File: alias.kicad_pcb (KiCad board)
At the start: 2 copper layers, 84.2 x 38.1 mm, 24 parts, among them SW1 SW_Push, U1 ATmega32U4-A, Y1 16MHz

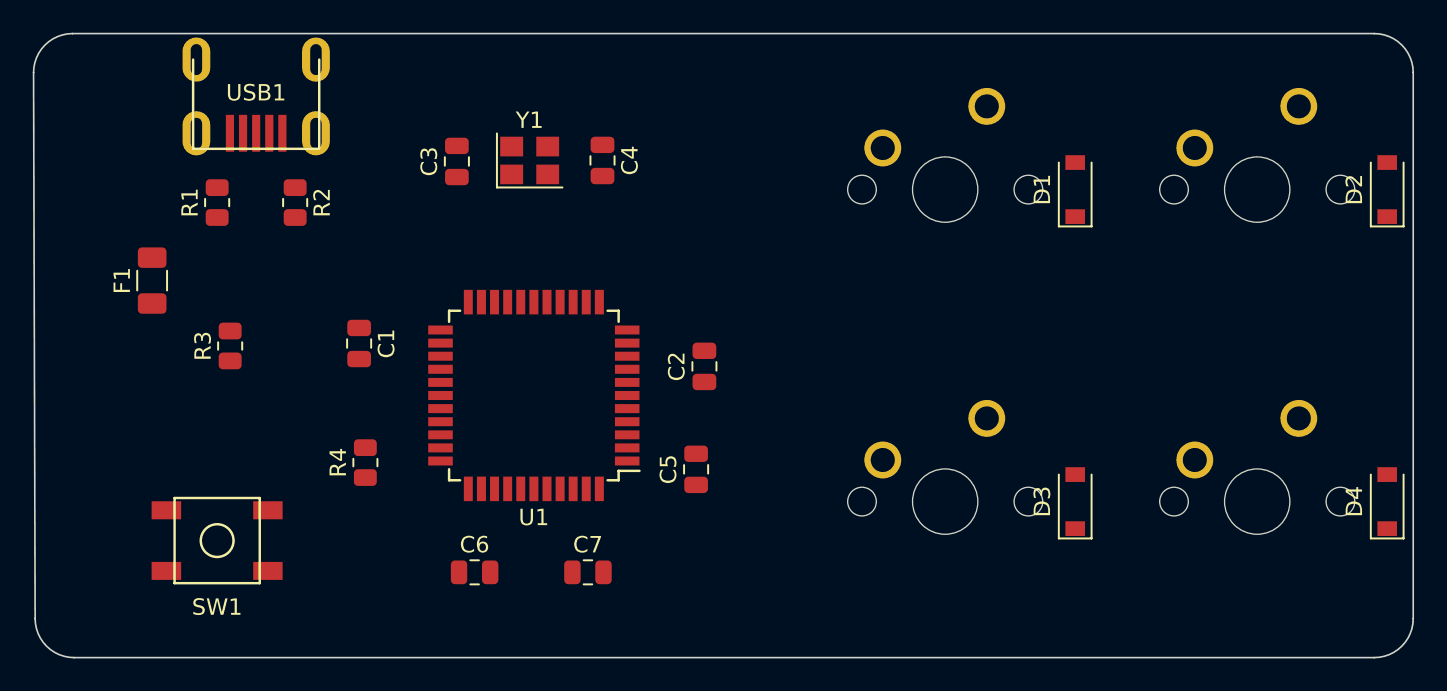
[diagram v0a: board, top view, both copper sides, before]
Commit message: Added routing (not finished)
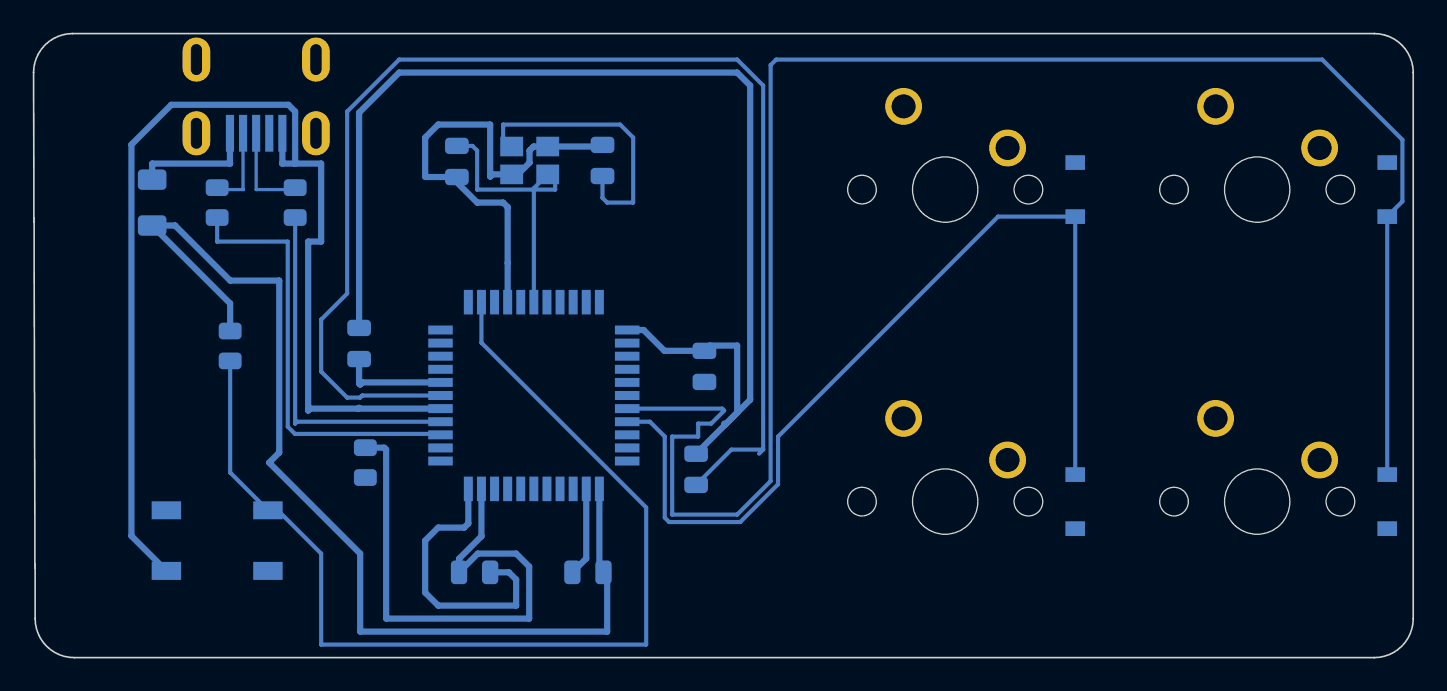
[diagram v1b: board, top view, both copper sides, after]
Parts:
- C1, C2, C3, C4, C5, C6, C7, D1, D2, D3, D4, F1, MX1, MX2, MX3, MX4, R1, R2, R3, R4, SW1, U1, USB1, Y1: moved to B.Cu
- moved F1 4.76 mm to (151.6, 89.7), turned to -90 degrees
- turned C1 to 90 degrees
- turned C6 to 180 degrees
- turned C7 to 180 degrees
- turned D3 to -90 degrees
- turned D4 to -90 degrees
- turned MX1 to 180 degrees
- turned MX2 to 180 degrees
- turned MX3 to 180 degrees
- turned MX4 to 180 degrees
- turned R1 to -90 degrees
- turned SW1 to 180 degrees
- turned U1 to 0 degrees
- turned Y1 to 180 degrees
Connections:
- D1 pad 1: ROW0 -> COL0
- D2 pad 1: ROW1 -> COL1
- D3 pad 1: ROW0 -> COL0
- D4 pad 1: ROW1 -> COL1
- MX1 pad 1: COL0 -> ROW0
- MX2 pad 1: COL0 -> ROW0
- MX3 pad 1: COL1 -> ROW1
- MX4 pad 1: COL1 -> ROW1
- U1 pad 29: unconnected-(U1-Pad29) -> COL1
- U1 pad 30: unconnected-(U1-Pad30) -> COL0
- U1 pad 31: unconnected-(U1-Pad31) -> ROW1
- U1 pad 32: unconnected-(U1-Pad32) -> ROW0
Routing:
- net GND: track 0.00 -> 214.2 mm
- net COL1: track 0.00 -> 108.9 mm
- net +5V: track 0.00 -> 89.7 mm
- net Net-(C5-Pad1): track 0.00 -> 79.8 mm
- net Net-(R3-Pad1): track 0.00 -> 64.9 mm
- net COL0: track 0.00 -> 58.0 mm
- net Net-(R1-Pad2): track 0.00 -> 26.6 mm
- net Net-(R2-Pad2): track 0.00 -> 21.5 mm
- net Net-(C3-Pad2): track 0.00 -> 17.8 mm
- net Net-(C4-Pad2): track 0.00 -> 17.1 mm
- net VCC: track 0.00 -> 7.60 mm
- net D+: track 0.00 -> 5.87 mm
- net D-: track 0.00 -> 5.08 mm
